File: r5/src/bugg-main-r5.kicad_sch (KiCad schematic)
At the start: 44 parts, among them T14 , T15 , T16 , T3 , T39 , T40 , U1 74LVC1G07DCK, U34 74LVC1G157GV

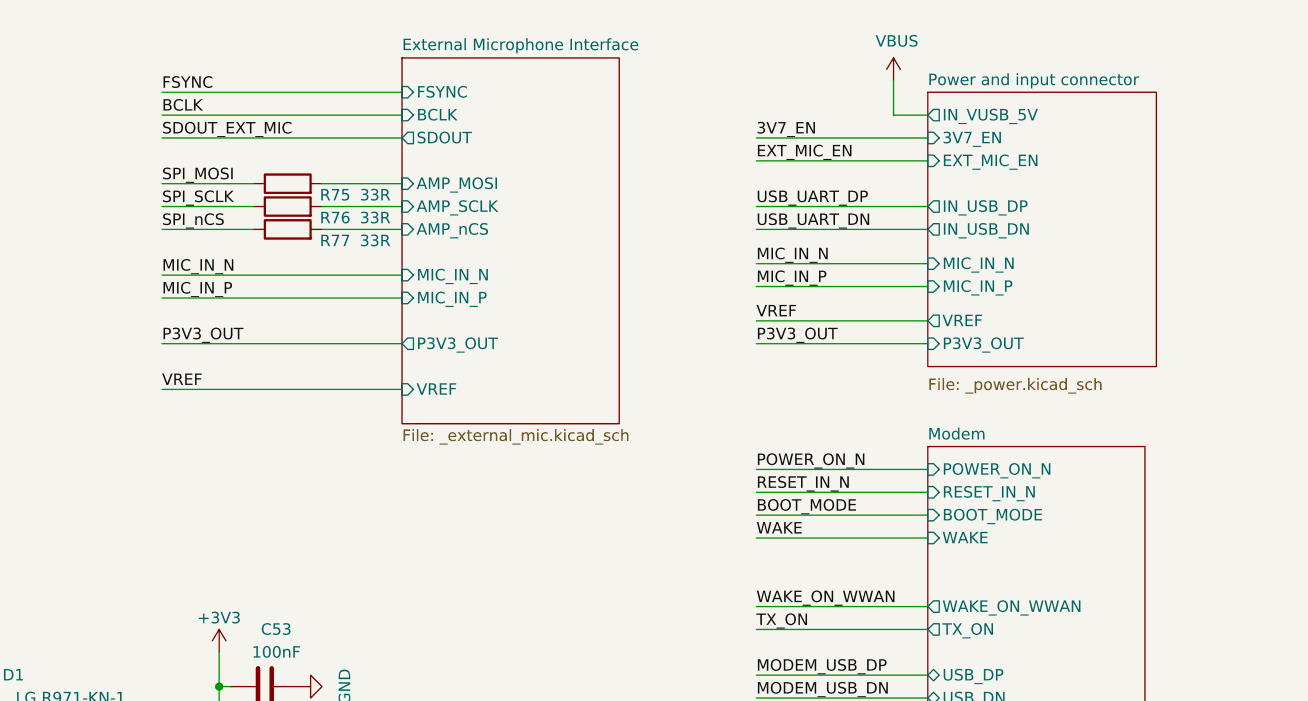
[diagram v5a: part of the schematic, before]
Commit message: Reestablish GND routing around amp control IC
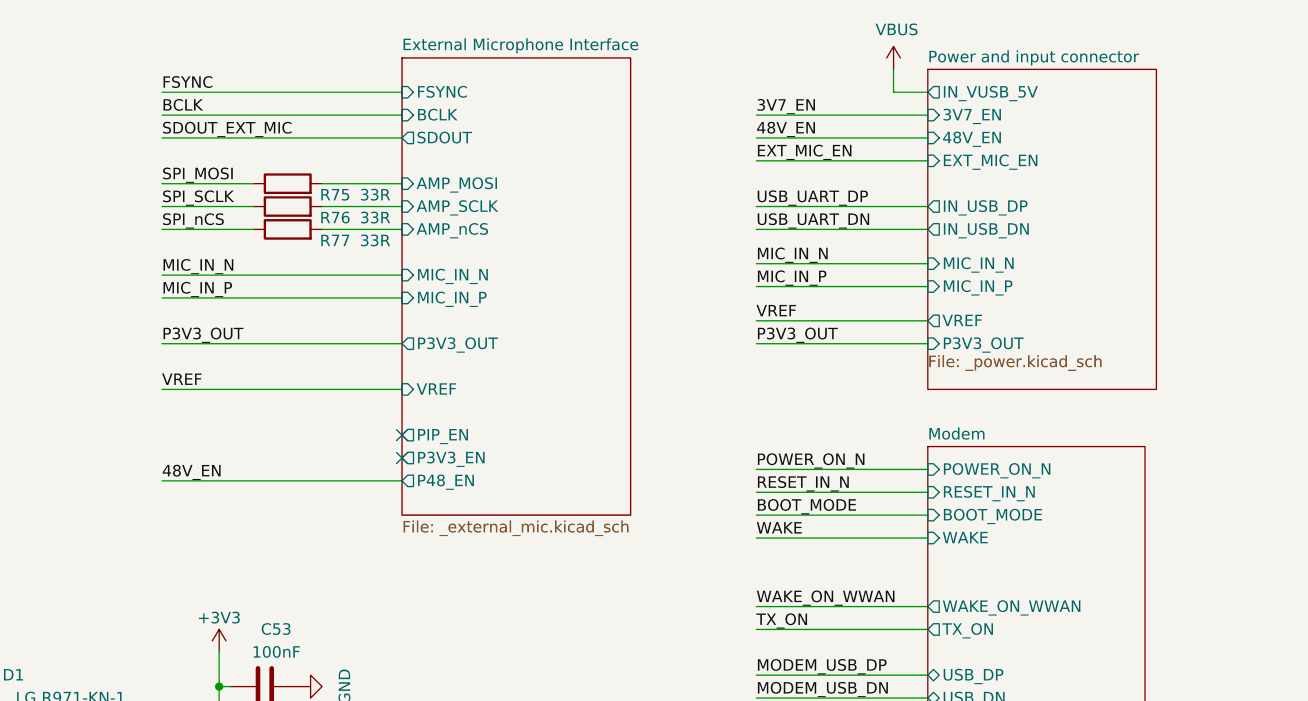
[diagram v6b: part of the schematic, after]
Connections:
- no-connect marks 136 -> 138
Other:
- sheet External Microphone Interface ports: added P3V3_EN, P48_EN, PIP_EN; removed none
- sheet Power and input connector ports: added 48V_EN; removed none
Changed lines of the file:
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@@
   (no_connect (at 113.03 149.86))
   (no_connect (at 52.07 195.58))
+  (no_connect (at 303.53 67.31))
   (no_connect (at 123.19 266.7))
   (no_connect (at 113.03 195.58))
@@
   (no_connect (at 240.03 165.1))
   (no_connect (at 240.03 167.64))
+  (no_connect (at 303.53 64.77))
   (no_connect (at 52.07 149.86))
   (no_connect (at 113.03 104.14))
@@
     (stroke (width 0) (type solid))
   )
-  (wire (pts (xy 358.14 25.4) (xy 358.14 29.21))
+  (wire (pts (xy 358.14 24.13) (xy 358.14 26.67))
     (stroke (width 0) (type solid))
   )
-  (wire (pts (xy 358.14 29.21) (xy 361.95 29.21))
+  (wire (pts (xy 358.14 26.67) (xy 361.95 26.67))
     (stroke (width 0) (type solid))
   )
@@
     (stroke (width 0) (type solid))
   )
+  (wire (pts (xy 342.9 31.75) (xy 361.95 31.75))
+    (stroke (width 0) (type default))
+  )
   (wire (pts (xy 240.03 124.46) (xy 264.16 124.46))
     (stroke (width 0) (type solid))
@@
     (stroke (width 0) (type solid))
   )
+  (wire (pts (xy 276.86 69.85) (xy 303.53 69.85))
+    (stroke (width 0) (type default))
+  )
   (wire (pts (xy 342.9 139.7) (xy 361.95 139.7))
     (stroke (width 0) (type solid))
@@
     (stroke (width 0) (type solid))
   )
-  (wire (pts (xy 342.9 31.75) (xy 361.95 31.75))
+  (wire (pts (xy 342.9 29.21) (xy 361.95 29.21))
     (stroke (width 0) (type solid))
   )
@@
     (effects (font (size 1.27 1.27)) (justify left bottom))
   )
+  (label "48V_EN" (at 276.86 69.85 0) (fields_autoplaced)
+    (effects (font (size 1.27 1.27)) (justify left bottom))
+  )
   (label "LED_USER" (at 156.21 106.68 0) (fields_autoplaced)
     (effects (font (size 1.27 1.27)) (justify left bottom))
@@
     (effects (font (size 1.27 1.27)) (justify left bottom))
   )
+  (label "48V_EN" (at 342.9 31.75 0) (fields_autoplaced)
+    (effects (font (size 1.27 1.27)) (justify left bottom))
+  )
   (label "3V7_EN" (at 264.16 119.38 180) (fields_autoplaced)
     (effects (font (size 1.27 1.27)) (justify right bottom))
@@
     (effects (font (size 1.27 1.27)) (justify right bottom))
   )
-  (label "3V7_EN" (at 342.9 31.75 0) (fields_autoplaced)
+  (label "3V7_EN" (at 342.9 29.21 0) (fields_autoplaced)
     (effects (font (size 1.27 1.27)) (justify left bottom))
   )
@@
     )
   )
-  (symbol (lib_id "power:VBUS") (at 358.14 25.4 0) (unit 1)
+  (symbol (lib_id "power:VBUS") (at 358.14 24.13 0) (unit 1)
     (exclude_from_sim no) (in_bom yes) (on_board yes) (dnp no)
-    (property "Reference" "#PWR040" (at 358.14 29.21 0)
+    (property "Reference" "#PWR040" (at 358.14 27.94 0)
       (effects (font (size 1.27 1.27)) hide)
     )
-    (property "Value" "VBUS" (at 358.521 21.0058 0)
+    (property "Value" "VBUS" (at 358.521 19.7358 0)
       (effects (font (size 1.27 1.27)))
     )
-    (property "Footprint" "" (at 358.14 25.4 0)
+    (property "Footprint" "" (at 358.14 24.13 0)
       (effects (font (size 1.27 1.27)) hide)
     )
-    (property "Datasheet" "" (at 358.14 25.4 0)
+    (property "Datasheet" "" (at 358.14 24.13 0)
       (effects (font (size 1.27 1.27)) hide)
     )
-    (property "Description" "" (at 358.14 25.4 0)
+    (property "Description" "" (at 358.14 24.13 0)
       (effects (font (size 1.27 1.27)) hide)
     )
@@
     )
   )
-  (sheet (at 303.53 22.86) (size 24.13 40.64) (fields_autoplaced)
+  (sheet (at 303.53 22.86) (size 25.4 50.8) (fields_autoplaced)
     (stroke (width 0.1524) (type solid) (color 132 0 132 1))
     (fill (color 255 255 255 0.0000))
@@
       (effects (font (size 1.27 1.27)) (justify left bottom))
     )
-    (property "Sheetfile" "_external_mic.kicad_sch" (at 303.53 64.0846 0)
+    (property "Sheetfile" "_external_mic.kicad_sch" (at 303.53 74.2446 0)
       (effects (font (size 1.27 1.27)) (justify left top))
     )
@@
       (effects (font (size 1.27 1.27)) (justify left))
     )
+    (pin "PIP_EN" output (at 303.53 64.77 180)
+      (effects (font (size 1.27 1.27)) (justify left))
+    )
+    (pin "P48_EN" output (at 303.53 69.85 180)
+      (effects (font (size 1.27 1.27)) (justify left))
+    )
+    (pin "P3V3_EN" output (at 303.53 67.31 180)
+      (effects (font (size 1.27 1.27)) (justify left))
+    )
     (instances
       (project "bugg-main-r5"
@@
     )
   )
-  (sheet (at 361.95 26.67) (size 25.4 30.48)
+  (sheet (at 361.95 24.13) (size 25.4 35.56)
     (stroke (width 0.001) (type solid) (color 132 0 132 1))
     (fill (color 255 255 255 0.0000))
-    (property "Sheetname" "Power and input connector" (at 361.95 26.0341 0)
+    (property "Sheetname" "Power and input connector" (at 361.95 23.4941 0)
       (effects (font (size 1.27 1.27)) (justify left bottom))
     )
-    (property "Sheetfile" "_power.kicad_sch" (at 361.95 58.42 0)
+    (property "Sheetfile" "_power.kicad_sch" (at 361.95 55.88 0)
       (effects (font (size 1.27 1.27)) (justify left top))
     )
-    (pin "3V7_EN" input (at 361.95 31.75 180)
+    (pin "3V7_EN" input (at 361.95 29.21 180)
       (effects (font (size 1.27 1.27)) (justify left))
     )
-    (pin "IN_VUSB_5V" output (at 361.95 29.21 180)
+    (pin "IN_VUSB_5V" output (at 361.95 26.67 180)
       (effects (font (size 1.27 1.27)) (justify left))
     )
@@
       (effects (font (size 1.27 1.27)) (justify left))
     )
+    (pin "48V_EN" input (at 361.95 31.75 180)
+      (effects (font (size 1.27 1.27)) (justify left))
+    )

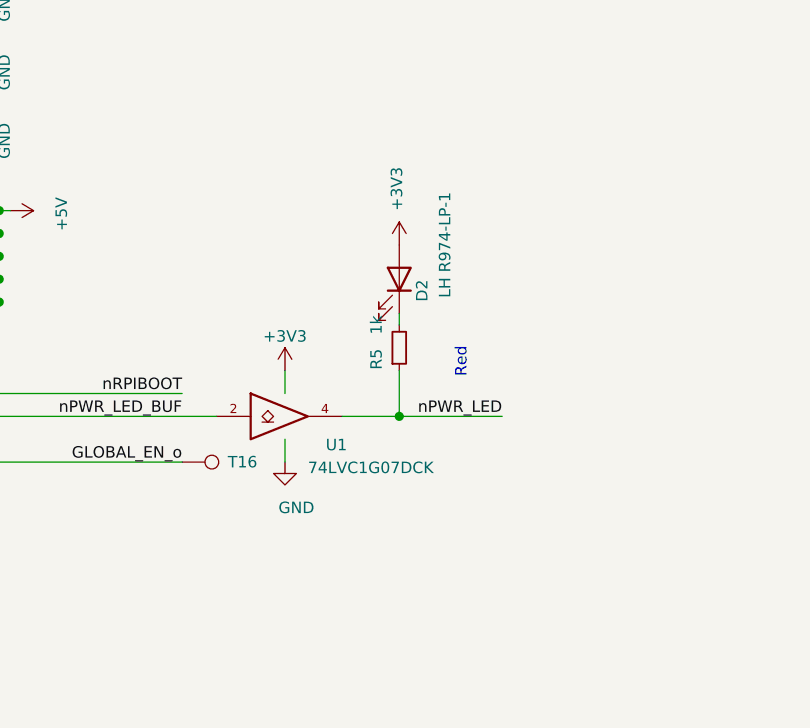
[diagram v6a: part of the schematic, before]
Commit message: Update schematic to include the latest library symbols. Mainly this updated the symbol fields, but three symbols actually changed, which required schematic edits to reconnect their pins. No circuit changes were made, and this was verified by checking the preview data in the PCB's "Update PCB from Schematic..." dialog.
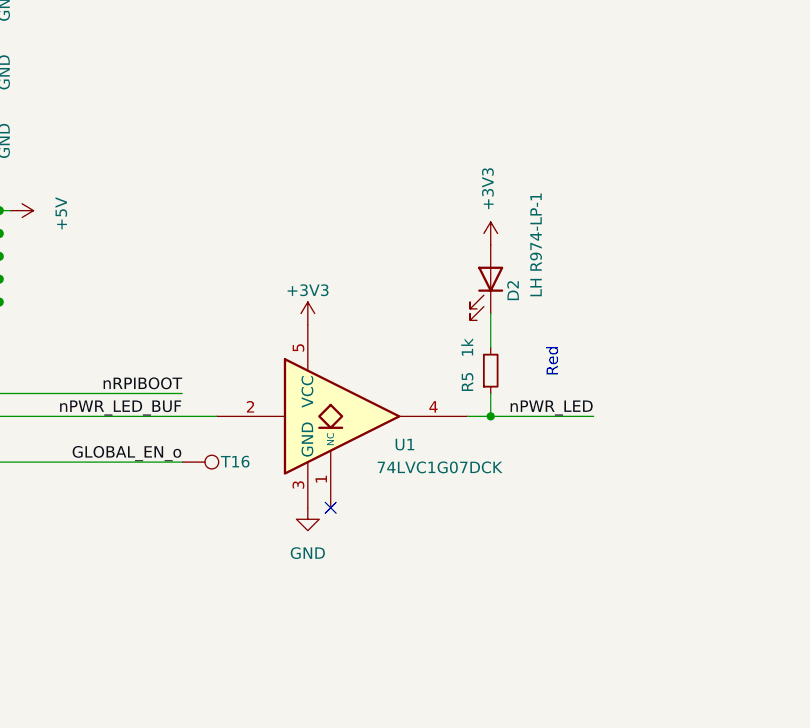
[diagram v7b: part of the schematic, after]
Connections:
- no-connect marks 138 -> 139
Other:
- moved on the sheet: D2, R5

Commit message: Exclude all testpoints from BoM
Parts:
- T14, T15, T16, T3, T39, T40: now left out of the parts list
